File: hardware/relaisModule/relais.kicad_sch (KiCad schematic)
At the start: 104 parts, among them J1 Button-Sensors-MicroMatch2X03, J10 WAGO2604-1104, J11 WAGO2604-1104, J12 RJ45-CAN, J13 WAGO2604-1102, J2 WAGO2604-1104, J4 WAGO2604-1104, J5 IRDA, J6 IRDA, J7 RJ45-CAN, J8 WAGO2604-1104, J9 WAGO2604-1104, K1 RT314A12, K10 RT314A12, K11 RT314A12, K12 RT314A12, K2 RT314A12, K3 RT314A12, K4 RT314A12, K5 RT314A12, K6 RT314A12, K7 RT314A12, K8 RT314A12, K9 RT314A12, Q1 BC847, Q2 BC847, U1 PESD2CAN, U2 MCP2562-E-SN, U3 ESP32-WROOM-32, U4 MCP1703A-3302_SOT89, U5 PCF8574A, U6 PCF8574A, U7 TPL7407LADR, U8 TPL7407LADR, U9 wuerthDebug6

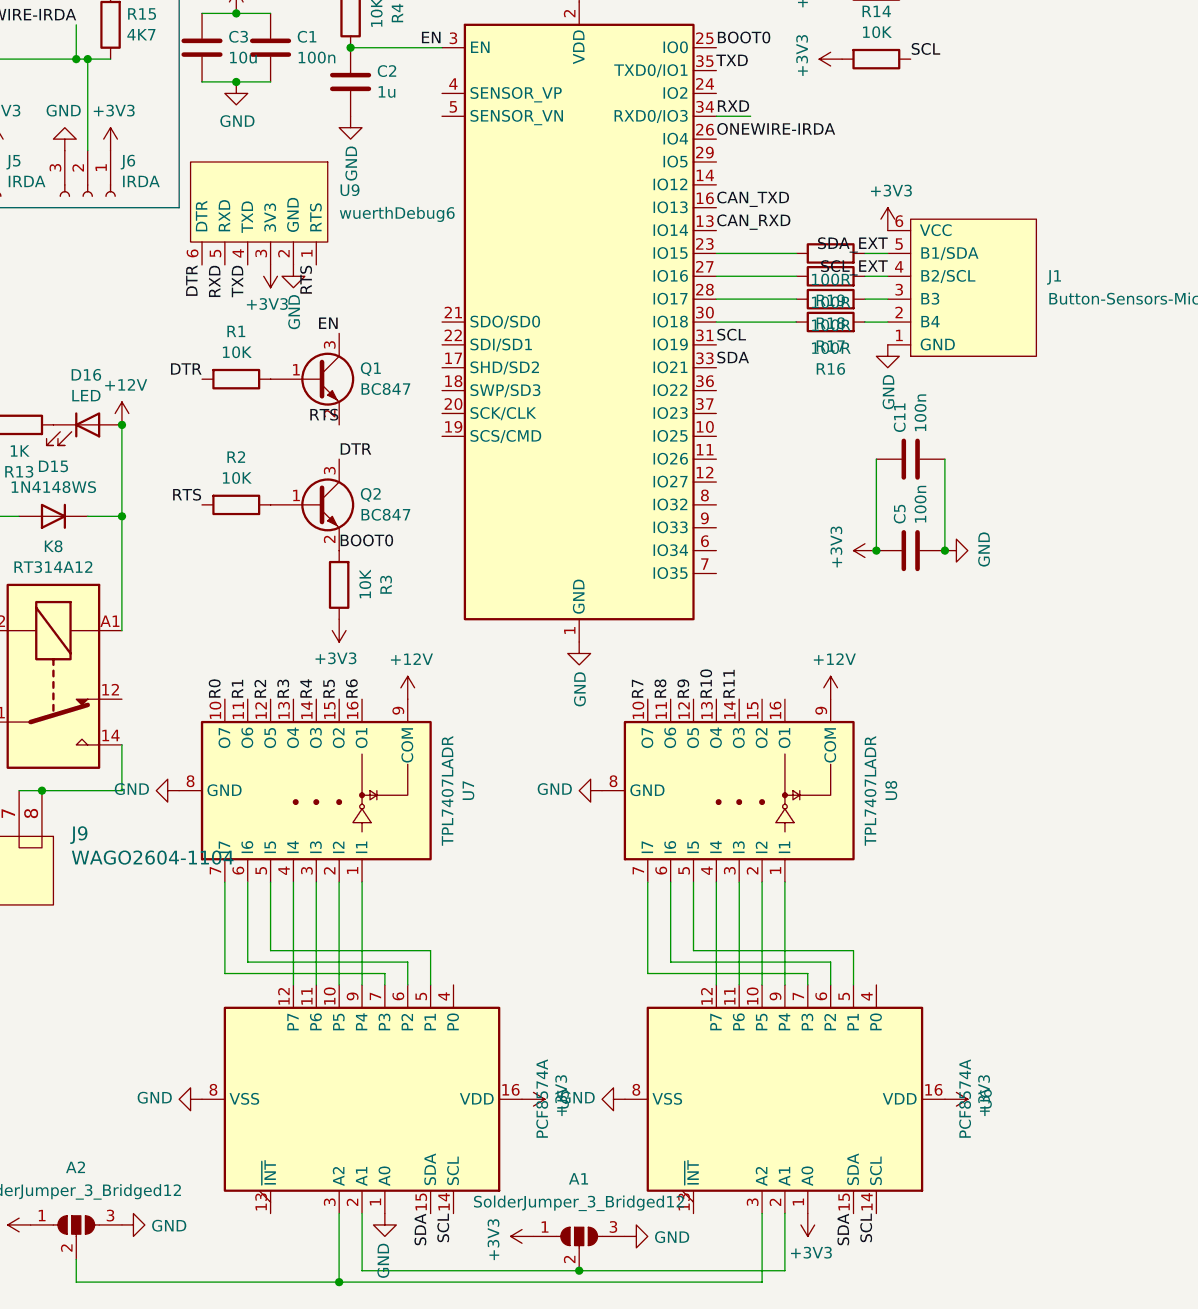
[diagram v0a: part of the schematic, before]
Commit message: feat: change PCB debug to EN/BOOT0
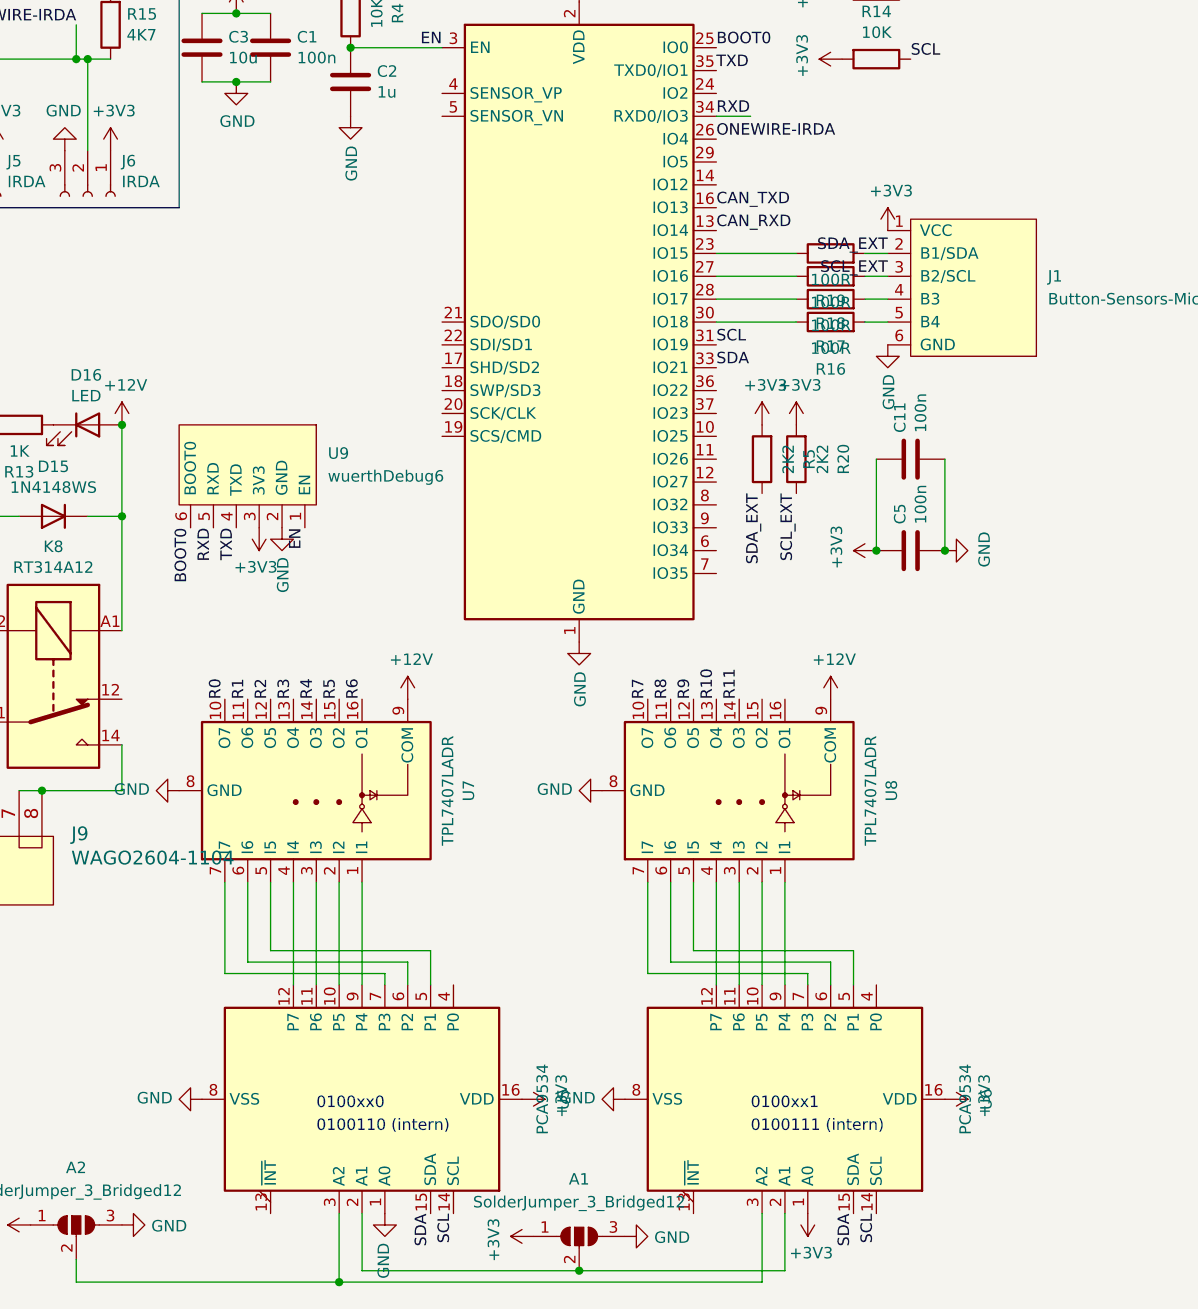
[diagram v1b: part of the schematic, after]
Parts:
- removed Q1, Q2: BC847, Package_TO_SOT_SMD:SOT-23, symbol Transistor_BJT:BC847
- removed R1, R2, R3: 10K, Resistor_SMD:R_0805_2012Metric_Pad1.20x1.40mm_HandSolder, symbol Device:R
- added R20, R5: 2K2, Resistor_SMD:R_0603_1608Metric_Pad0.98x0.95mm_HandSolder, symbol Device:R
- C1, C10, C11, C2, C4, C5, C8, C9: footprint Capacitor_SMD:C_0805_2012Metric_Pad1.18x1.45mm_HandSolder -> Capacitor_SMD:C_0603_1608Metric_Pad1.08x0.95mm_HandSolder
- D10, D12, D14, D16, D18, D2, D20, D22, D24, D4, D6, D8: footprint LED_SMD:LED_0805_2012Metric_Pad1.15x1.40mm_HandSolder -> LED_SMD:LED_0603_1608Metric_Pad1.05x0.95mm_HandSolder
- H1, H2, H3, H5: footprint MountingHole:MountingHole_4.3mm_M4_DIN965 -> MountingHole:MountingHole_3.2mm_M3_DIN965
- R10, R11, R12, R13, R14, R15, R16, R17, R18, R19, R21, R22, R23, R24, R25, R27, R4, R6, R7, R8, R9: footprint Resistor_SMD:R_0805_2012Metric_Pad1.20x1.40mm_HandSolder -> Resistor_SMD:R_0603_1608Metric_Pad0.98x0.95mm_HandSolder
- U5, U6: value PCF8574A -> PCA9534
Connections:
- net DTR is gone; now on net BOOT0: U9.6 (BOOT0)
- net RTS is gone; now on net EN: U9.1 (EN)
- net +3V3: now also J1.1 (VCC), R20.2, R5.2; no longer J1.6 (VCC)
- net GND: now also J1.6 (GND); no longer J1.1 (GND)
- net SCL_EXT: now also J1.3 (B2/SCL), R20.1; no longer J1.4 (B2/SCL)
- net SDA_EXT: now also J1.2 (B1/SDA), R5.1; no longer J1.5 (B1/SDA)
- net at R16.2: now also J1.5 (B4); no longer J1.2 (B4)
- net at R17.2: now also J1.4 (B3); no longer J1.3 (B3)
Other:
- note added: "0100110 (intern)"
- note added: "0100111 (intern)"
- note added: "0100xx0"
- note added: "0100xx1"
- moved on the sheet: U9
